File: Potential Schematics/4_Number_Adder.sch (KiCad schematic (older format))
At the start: 0 parts

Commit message: Made Multiplier
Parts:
- added U? (x2): 74LS32, symbol 4-bit_processor-rescue:74LS32
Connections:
- new net: U?.2, U?.3
- new net Cout: U?.3
- new net GND: U?.7 (GND), U?.7 (GND)
- new net VCC: U?.14 (VCC), U?.14 (VCC)
- new net sheet5BABD82C/Cout: U?.1
- new net sheet5BABD853/Cout: U?.2
- new net sheet5BABD8A3/Cout: U?.1
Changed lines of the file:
@@
 $Descr A4 11693 8268
 encoding utf-8
-Sheet 458 458
+Sheet 457 467
 Title ""
 Date ""
@@
 s
 Text HLabel 8750 3650 2    50   Output ~ 0
-Cout0
-Text HLabel 8750 3750 2    50   Output ~ 0
-Cout1
+Cout
+$Sheet
+S 3150 3500 550  350
+U 5BABD833
+F0 "sheet5BABD82C" 60
+F1 "Full_adder.sch" 60
+F2 "a" I L 3150 3650 60
+F3 "b" I L 3150 3750 60
+F4 "Cin" I L 3150 3550 60
+F5 "S" O R 3700 3550 60
+F6 "Cout" O R 3700 3650 60
+$EndSheet
+Wire Wire Line
+	2150 3550 3150 3550
+Wire Wire Line
+	2150 3650 3150 3650
+Wire Wire Line
+	2150 3750 3150 3750
+$Sheet
+S 4350 3500 550  250
+U 5BABD859
+F0 "sheet5BABD853" 50
+F1 "Half_Adder.sch" 50
+F2 "a" I L 4350 3550 50
+F3 "b" I L 4350 3650 50
+F4 "s" O R 4900 3550 50
+F5 "Cout" O R 4900 3650 50
+$EndSheet
+$Sheet
+S 5700 3500 550  250
+U 5BABD8A9
+F0 "sheet5BABD8A3" 50
+F1 "Half_Adder.sch" 50
+F2 "a" I L 5700 3550 50
+F3 "b" I L 5700 3650 50
+F4 "s" O R 6250 3550 50
+F5 "Cout" O R 6250 3650 50
+$EndSheet
+Wire Wire Line
+	2150 3850 2850 3850
+Wire Wire Line
+	2850 3850 2850 4000
+Wire Wire Line
+	2850 4000 4200 4000
+Wire Wire Line
+	4200 4000 4200 3650
+Wire Wire Line
+	4200 3650 4350 3650
+Wire Wire Line
+	2150 3950 2650 3950
+Wire Wire Line
+	2650 3950 2650 4050
+Wire Wire Line
+	2650 4050 5450 4050
+Wire Wire Line
+	5450 4050 5450 3650
+Wire Wire Line
+	5450 3650 5700 3650
+Wire Wire Line
+	6250 3550 8750 3550
+Wire Wire Line
+	3700 3550 4350 3550
+Wire Wire Line
+	4900 3550 5700 3550
+$Comp
+L 4-bit_processor-rescue:74LS32 U?
+U 1 1 5BABDE29
+P 5650 4650
+F 0 "U?" H 5650 5016 50  0000 C CNN
+F 1 "74LS32" H 5650 4925 50  0000 C CNN
+F 2 "" H 5650 4650 50  0001 C CNN
+F 3 "" H 5650 4650 50  0001 C CNN
+	1    5650 4650
+	1    0    0    -1
+$EndComp
+$Comp
+L 4-bit_processor-rescue:74LS32 U?
+U 1 1 5BABDF06
+P 7300 4550
+F 0 "U?" H 7300 4916 50  0000 C CNN
+F 1 "74LS32" H 7300 4825 50  0000 C CNN
+F 2 "" H 7300 4550 50  0001 C CNN
+F 3 "" H 7300 4550 50  0001 C CNN
+	1    7300 4550
+	1    0    0    -1
+$EndComp
+Wire Wire Line
+	3700 3650 4100 3650
+Wire Wire Line
+	4100 3650 4100 4550
+Wire Wire Line
+	4100 4550 5050 4550
+Wire Wire Line
+	4900 3650 4950 3650
+Wire Wire Line
+	4950 3650 4950 4750
+Wire Wire Line
+	4950 4750 5050 4750
+Wire Wire Line
+	6250 4650 6700 4650
+Wire Wire Line
+	6700 4450 6700 3650
+Wire Wire Line
+	6700 3650 6250 3650
+Wire Wire Line
+	7900 4550 7900 3650
+Wire Wire Line
+	7900 3650 8750 3650
 $EndSCHEMATC

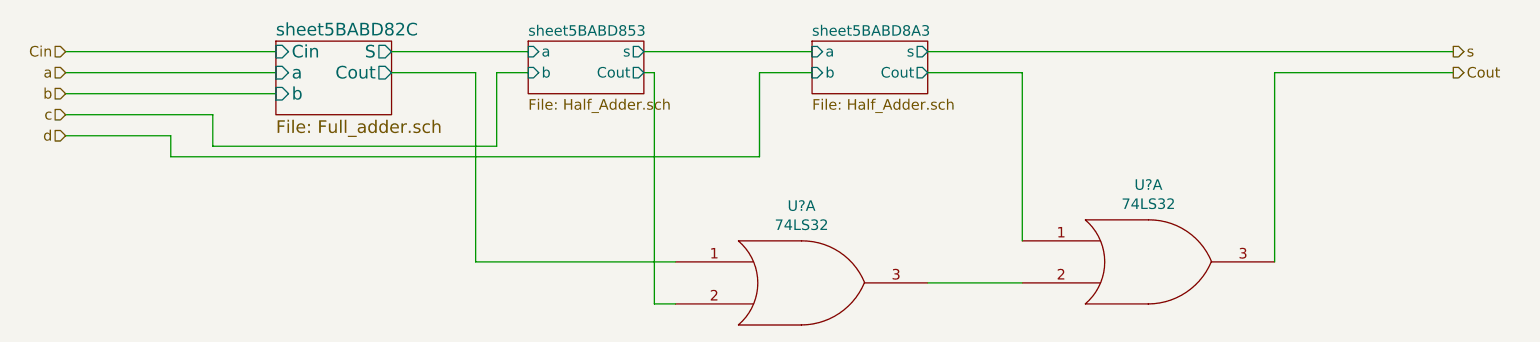
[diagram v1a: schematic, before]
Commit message: Updated overview of Schematic
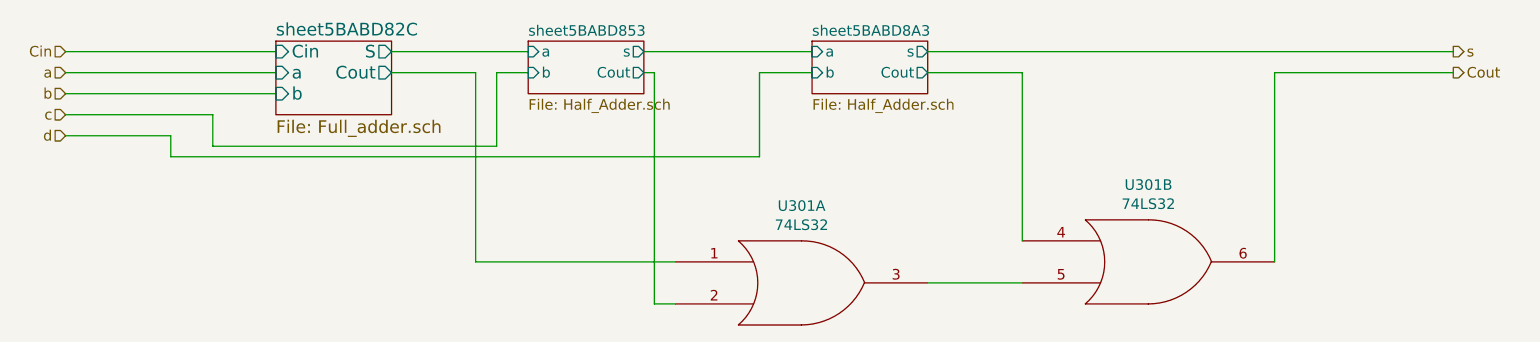
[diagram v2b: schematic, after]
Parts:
- gave numbers to parts that had none: 1
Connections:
- net Cout: now also U301.6; no longer U301.3
- net sheet5BABD8A3/Cout: now also U301.4; no longer U301.1
- net at U301.3: now also U301.5; no longer U301.2
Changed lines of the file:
@@
 $Descr A4 11693 8268
 encoding utf-8
-Sheet 457 467
+Sheet 457 902
 Title ""
 Date ""
@@
 U 1 1 5BABDE29
 P 5650 4650
-F 0 "U?" H 5650 5016 50  0000 C CNN
+AR Path="/5B9D167A/5BAA33A0/5BAAE2A8/5BABDE29" Ref="U?"  Part="1"
+AR Path="/5B9D167A/5BAA33A0/5BAFDB78/5BAFDE46/5BABDE29" Ref="U301"  Part="1"
+F 0 "U301" H 5650 5016 50  0000 C CNN
 F 1 "74LS32" H 5650 4925 50  0000 C CNN
 F 2 "" H 5650 4650 50  0001 C CNN
@@
 $Comp
 L 4-bit_processor-rescue:74LS32 U?
-U 1 1 5BABDF06
+U 2 1 5BABDF06
 P 7300 4550
-F 0 "U?" H 7300 4916 50  0000 C CNN
+AR Path="/5B9D167A/5BAA33A0/5BAAE2A8/5BABDF06" Ref="U?"  Part="1"
+AR Path="/5B9D167A/5BAA33A0/5BAFDB78/5BAFDE46/5BABDF06" Ref="U301"  Part="2"
+F 0 "U301" H 7300 4916 50  0000 C CNN
 F 1 "74LS32" H 7300 4825 50  0000 C CNN
 F 2 "" H 7300 4550 50  0001 C CNN
 F 3 "" H 7300 4550 50  0001 C CNN
-	1    7300 4550
+	2    7300 4550
 	1    0    0    -1
 $EndComp
